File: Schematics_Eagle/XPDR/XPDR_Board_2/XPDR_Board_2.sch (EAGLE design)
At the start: 29 parts

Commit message: Both XPDR boards finished.
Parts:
- U$1, U$2, U$3, U$4: device RadioStack_v2:LS7084 -> library:LS7084
- U$10, U$12, U$13, U$14, U$17, U$18, U$19, U$20, U$21, U$22, U$23, U$24, U$8: device RadioStack_v2:REZISTOR -> library:REZISTOR
- U$11: device RadioStack_v2:ADRESA_0..2 -> library:ADRESA_0..2
- U$15, U$25, U$26, U$28, U$29: device RadioStack_v2:KONDENZATOR -> library:KONDENZATOR
- U$16: device RadioStack_v2:ROTARY_SWITCH -> library:ROTARY_SWITCH
- U$27, U$5: device RadioStack_v2:LISTA_2X5 -> library:LISTA_2X5
- U$6: device RadioStack_v2:ICM7228A -> library:ICM7228A
- U$7: device RadioStack_v2:LISTA_2X10 -> library:LISTA_2X10
- U$9: device RadioStack_v2:MCP23016 -> library:MCP23016
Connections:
- net GND: now also U$5.6; no longer U$5.1
- net N$12: now also U$5.7; no longer U$5.2
- net N$44: now also U$5.9; no longer U$5.4
- net N$45: now also U$5.10; no longer U$5.5
- net N$46: now also U$5.2; no longer U$5.9
- net N$47: now also U$5.1; no longer U$5.10
- net N$54: now also U$5.8; no longer U$5.7
- net N$55: now also U$5.4; no longer U$5.8
- net N$59: now also U$5.5; no longer U$5.6
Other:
- moved on the sheet: U$27

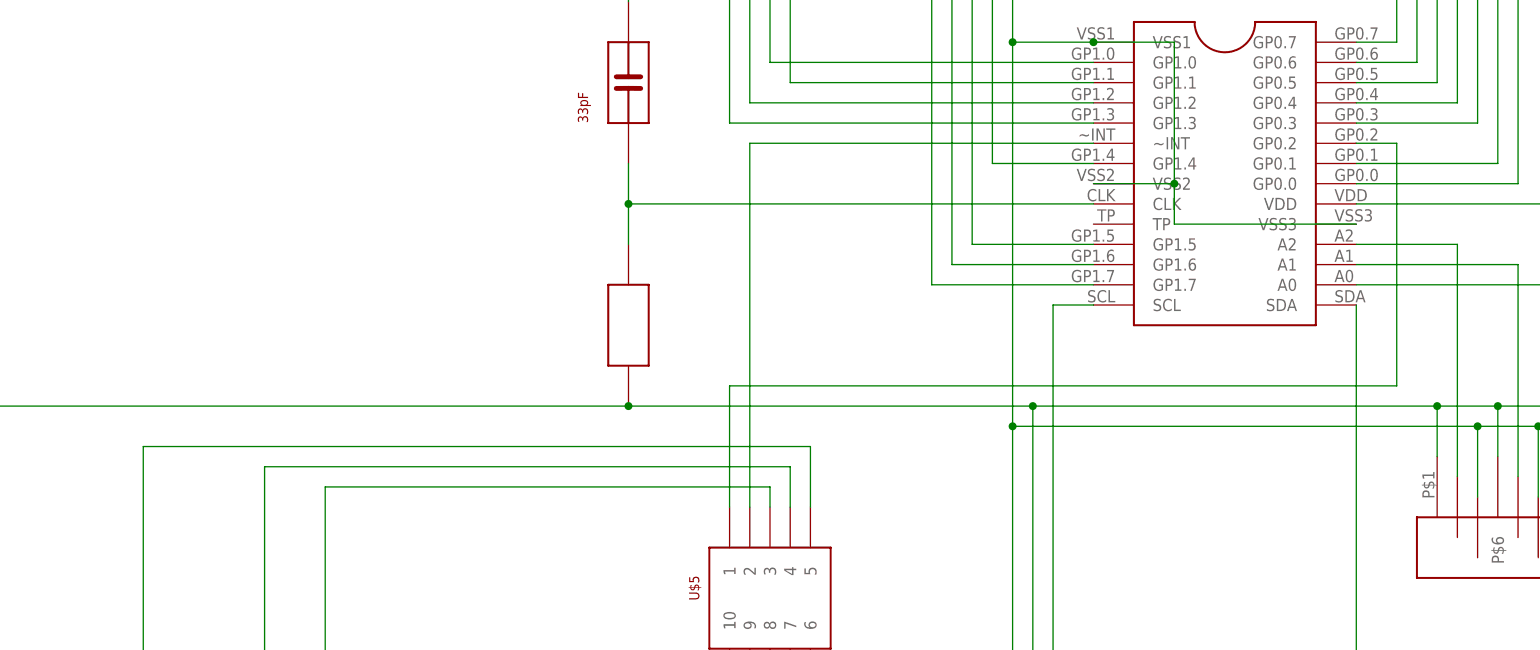
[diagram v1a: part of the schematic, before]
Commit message: - DME module finished. - Problem with incorrect pins (RST, INT) in XPDR module fixed.
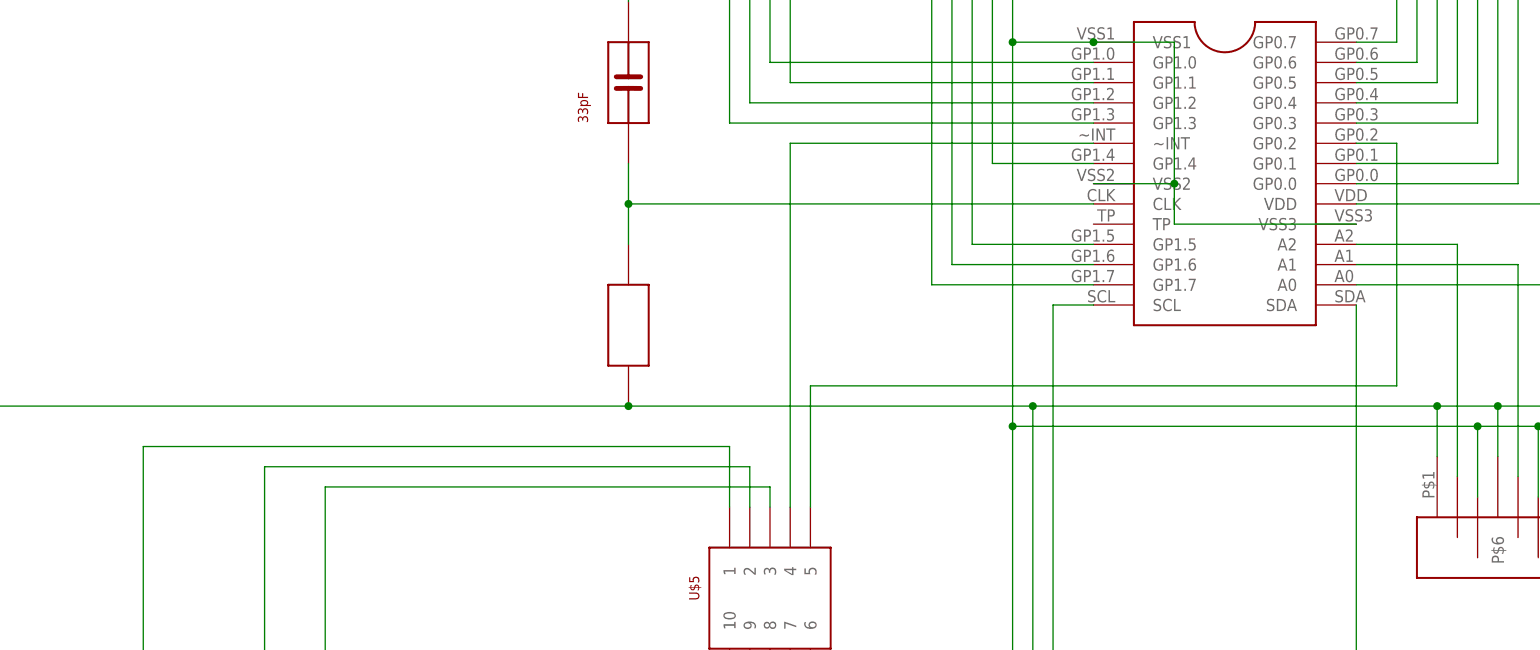
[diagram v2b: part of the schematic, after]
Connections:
- net N$46: now also U$5.4; no longer U$5.2
- net N$47: now also U$5.5; no longer U$5.1
- net N$55: now also U$5.2; no longer U$5.4
- net N$59: now also U$5.1; no longer U$5.5
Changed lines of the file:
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@@
 <segment>
 <pinref part="U$9" gate="G$1" pin="~INT"/>
-<wire x1="-426.72" y1="-116.84" x2="-426.72" y2="-71.12" width="0.1524" layer="91"/>
-<wire x1="-426.72" y1="-71.12" x2="-383.54" y2="-71.12" width="0.1524" layer="91"/>
-<pinref part="U$5" gate="G$2" pin="2"/>
+<wire x1="-421.64" y1="-71.12" x2="-383.54" y2="-71.12" width="0.1524" layer="91"/>
+<pinref part="U$5" gate="G$2" pin="4"/>
+<wire x1="-421.64" y1="-71.12" x2="-421.64" y2="-116.84" width="0.1524" layer="91"/>
 </segment>
 </net>
@@
 <pinref part="U$9" gate="G$1" pin="GP0.2"/>
 <wire x1="-345.44" y1="-71.12" x2="-350.52" y2="-71.12" width="0.1524" layer="91"/>
-<wire x1="-345.44" y1="-101.6" x2="-429.26" y2="-101.6" width="0.1524" layer="91"/>
-<pinref part="U$5" gate="G$2" pin="1"/>
-<wire x1="-429.26" y1="-101.6" x2="-429.26" y2="-116.84" width="0.1524" layer="91"/>
+<wire x1="-345.44" y1="-101.6" x2="-419.1" y2="-101.6" width="0.1524" layer="91"/>
+<wire x1="-419.1" y1="-101.6" x2="-419.1" y2="-116.84" width="0.1524" layer="91"/>
+<pinref part="U$5" gate="G$2" pin="5"/>
 </segment>
 </net>
@@
 <segment>
 <wire x1="-487.68" y1="-149.86" x2="-487.68" y2="-111.76" width="0.1524" layer="91"/>
-<wire x1="-487.68" y1="-111.76" x2="-421.64" y2="-111.76" width="0.1524" layer="91"/>
+<wire x1="-487.68" y1="-111.76" x2="-426.72" y2="-111.76" width="0.1524" layer="91"/>
 <pinref part="U$22" gate="G$1" pin="P$1"/>
 <wire x1="-508" y1="-149.86" x2="-487.68" y2="-149.86" width="0.1524" layer="91"/>
@@
 <wire x1="-487.68" y1="-170.18" x2="-487.68" y2="-149.86" width="0.1524" layer="91"/>
 <junction x="-487.68" y="-149.86"/>
-<pinref part="U$5" gate="G$2" pin="4"/>
-<wire x1="-421.64" y1="-111.76" x2="-421.64" y2="-116.84" width="0.1524" layer="91"/>
+<pinref part="U$5" gate="G$2" pin="2"/>
+<wire x1="-426.72" y1="-111.76" x2="-426.72" y2="-116.84" width="0.1524" layer="91"/>
 </segment>
 </net>
@@
 <wire x1="-508" y1="-165.1" x2="-502.92" y2="-165.1" width="0.1524" layer="91"/>
 <wire x1="-502.92" y1="-165.1" x2="-502.92" y2="-109.22" width="0.1524" layer="91"/>
-<wire x1="-502.92" y1="-109.22" x2="-419.1" y2="-109.22" width="0.1524" layer="91"/>
+<wire x1="-502.92" y1="-109.22" x2="-429.26" y2="-109.22" width="0.1524" layer="91"/>
 <pinref part="U$25" gate="G$1" pin="P$2"/>
 <wire x1="-502.92" y1="-170.18" x2="-502.92" y2="-165.1" width="0.1524" layer="91"/>
 <junction x="-502.92" y="-165.1"/>
-<pinref part="U$5" gate="G$2" pin="5"/>
-<wire x1="-419.1" y1="-109.22" x2="-419.1" y2="-116.84" width="0.1524" layer="91"/>
+<pinref part="U$5" gate="G$2" pin="1"/>
+<wire x1="-429.26" y1="-109.22" x2="-429.26" y2="-116.84" width="0.1524" layer="91"/>
 </segment>
 </net>
